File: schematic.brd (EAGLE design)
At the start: 100 x 70 mm, 44 parts, among them U1 ADP3338AKCZ-3.3RL7

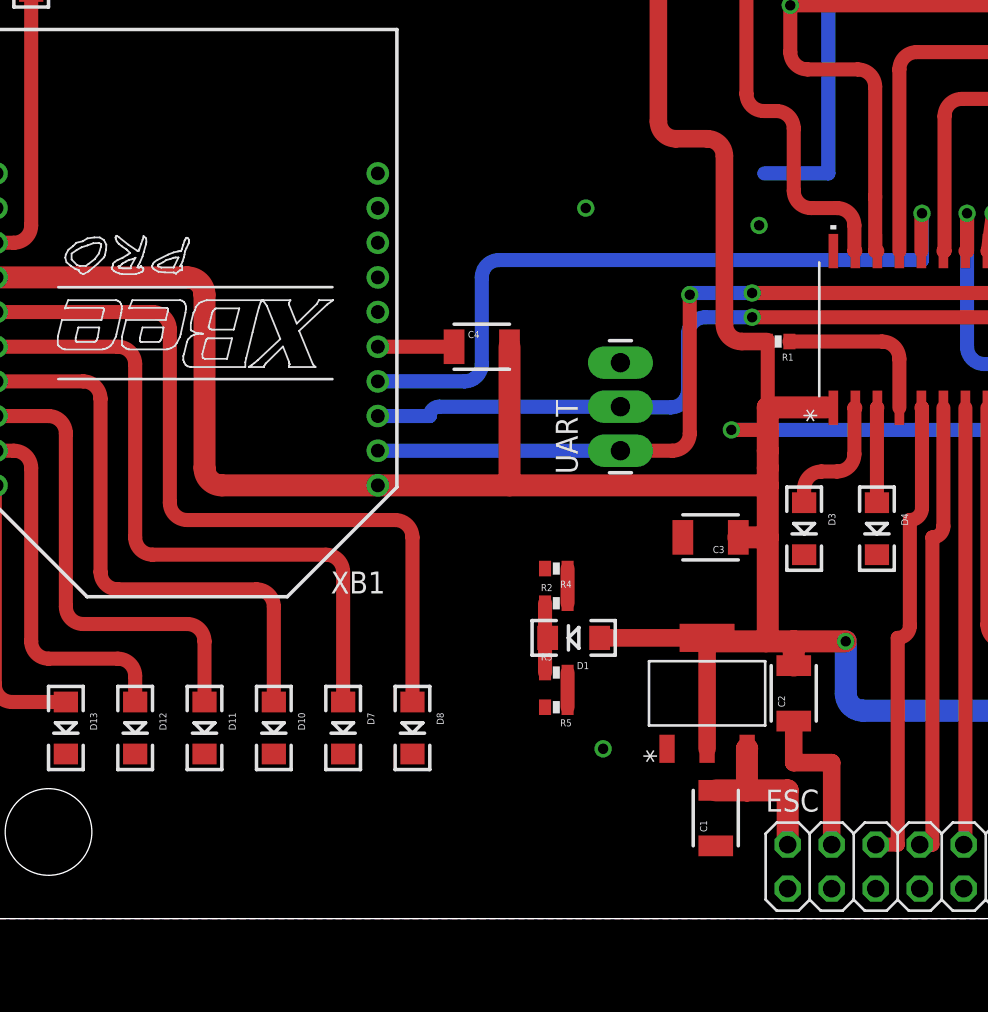
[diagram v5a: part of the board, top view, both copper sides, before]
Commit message: Added designer's name to pcb
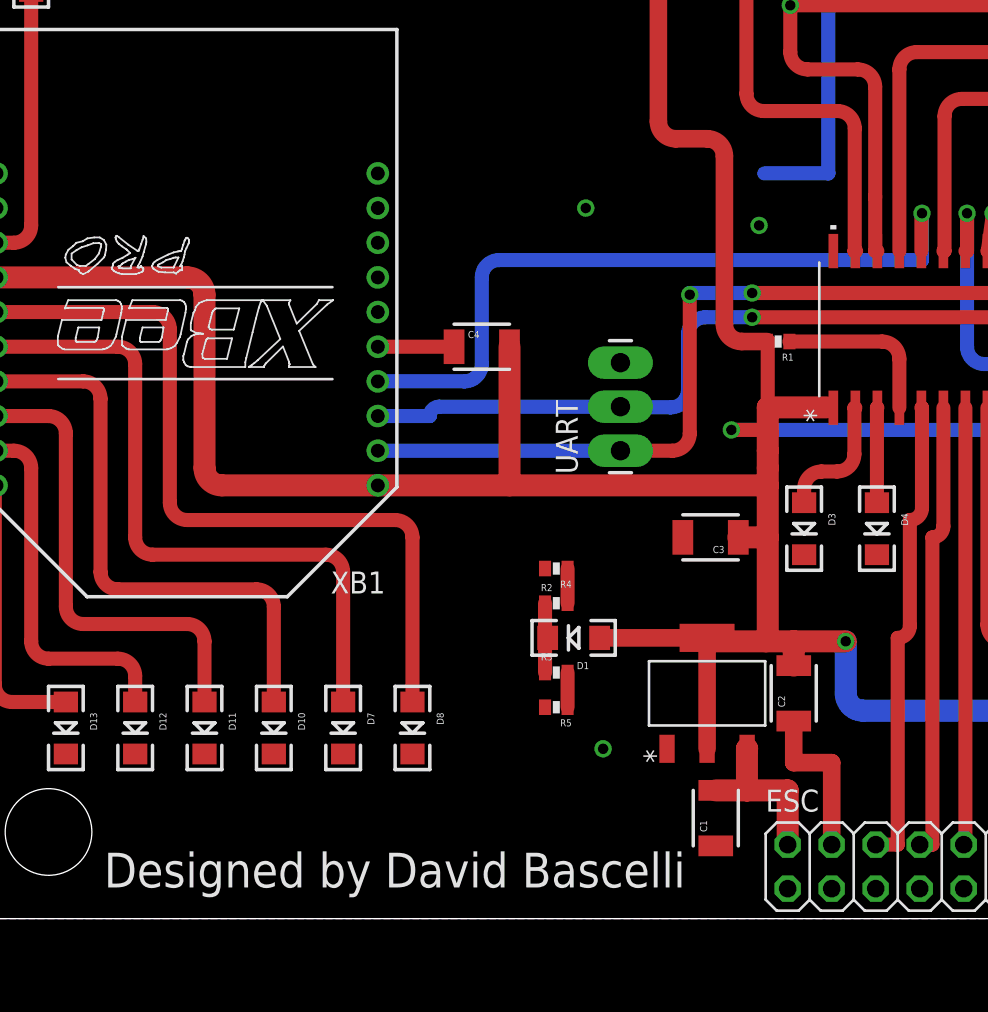
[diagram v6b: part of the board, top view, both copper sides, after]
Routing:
- net PGD/PITCH: track 57.0 -> 58.3 mm
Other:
- board text added: "Designed by David Bascelli"
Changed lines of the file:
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@@
 <rectangle x1="86.98" y1="19.7" x2="87.26" y2="19.74" layer="21" rot="R90"/>
 <rectangle x1="86.76" y1="42.76" x2="87.48" y2="42.8" layer="21" rot="R90"/>
+<text x="8.2" y="1.8" size="2" layer="21">Designed by David Bascelli</text>
 </plain>
 <attributes>
@@
 <contactref element="MAIN_CONTROLLER" pad="19"/>
 <wire x1="51.555" y1="38.5212" x2="51.5" y2="38.5212" width="0.8128" layer="1"/>
-<wire x1="47" y1="46.6" x2="46.27" y2="46.6" width="0.8128" layer="1"/>
 <wire x1="46.27" y1="46.6" x2="45.27" y2="47.6" width="0.8128" layer="1" curve="-90"/>
 <wire x1="45.27" y1="47.6" x2="45.27" y2="57.5" width="0.8128" layer="1"/>
 <wire x1="45.27" y1="57.5" x2="45.27" y2="68.19" width="0.8128" layer="1"/>
-<wire x1="48" y1="45.6" x2="48" y2="42" width="0.8128" layer="1"/>
-<wire x1="48" y1="42" x2="49" y2="41" width="0.8128" layer="1" curve="90"/>
-<wire x1="49" y1="41" x2="50.5" y2="41" width="0.8128" layer="1"/>
-<wire x1="50.5" y1="41" x2="51.5" y2="40" width="0.8128" layer="1" curve="-90"/>
-<wire x1="51.5" y1="40" x2="51.5" y2="38.5212" width="0.8128" layer="1"/>
-<wire x1="48" y1="45.6" x2="47" y2="46.6" width="0.8128" layer="1" curve="90"/>
 <wire x1="45.27" y1="57.5" x2="57.73" y2="57.5" width="0.8128" layer="1"/>
 <wire x1="57.73" y1="57.5" x2="58.73" y2="58.5" width="0.8128" layer="1" curve="90"/>
 <wire x1="58.73" y1="58.5" x2="58.73" y2="68" width="0.8128" layer="1"/>
+<wire x1="46.27" y1="46.6" x2="50.52" y2="46.6" width="0.8128" layer="1"/>
+<wire x1="50.52" y1="46.6" x2="51.52" y2="45.6" width="0.8128" layer="1" curve="-90"/>
+<wire x1="51.52" y1="45.6" x2="51.52" y2="38.52" width="0.8128" layer="1"/>
+<wire x1="51.52" y1="38.48" x2="51.52" y2="38.52" width="0.8128" layer="1"/>
+<wire x1="51.52" y1="38.52" x2="51.6" y2="38.52" width="0.8128" layer="1"/>
+<wire x1="51.52" y1="38.52" x2="51.5" y2="38.5212" width="0" layer="19" extent="1-1"/>
 </signal>
 <signal name="PGC/ROLL">

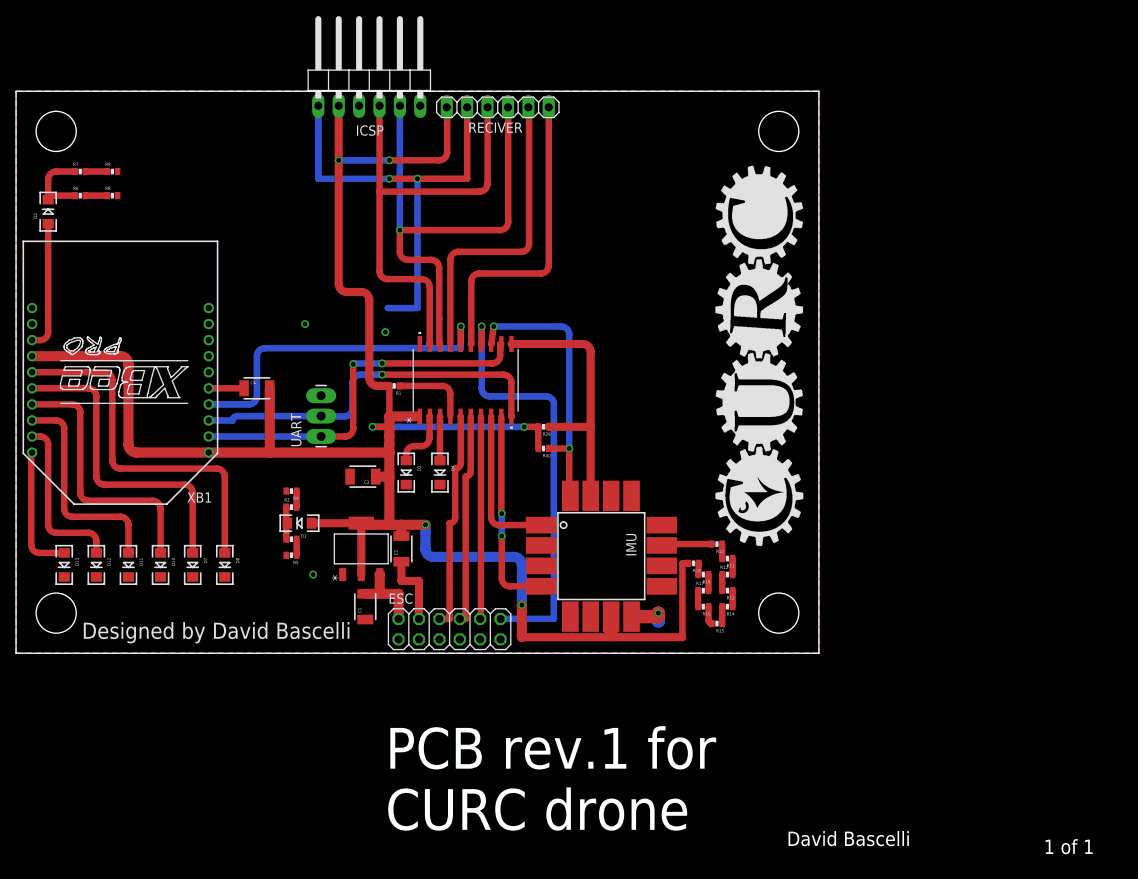
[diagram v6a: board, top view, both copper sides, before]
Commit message: Cleaned up the silkscreen and added more labels
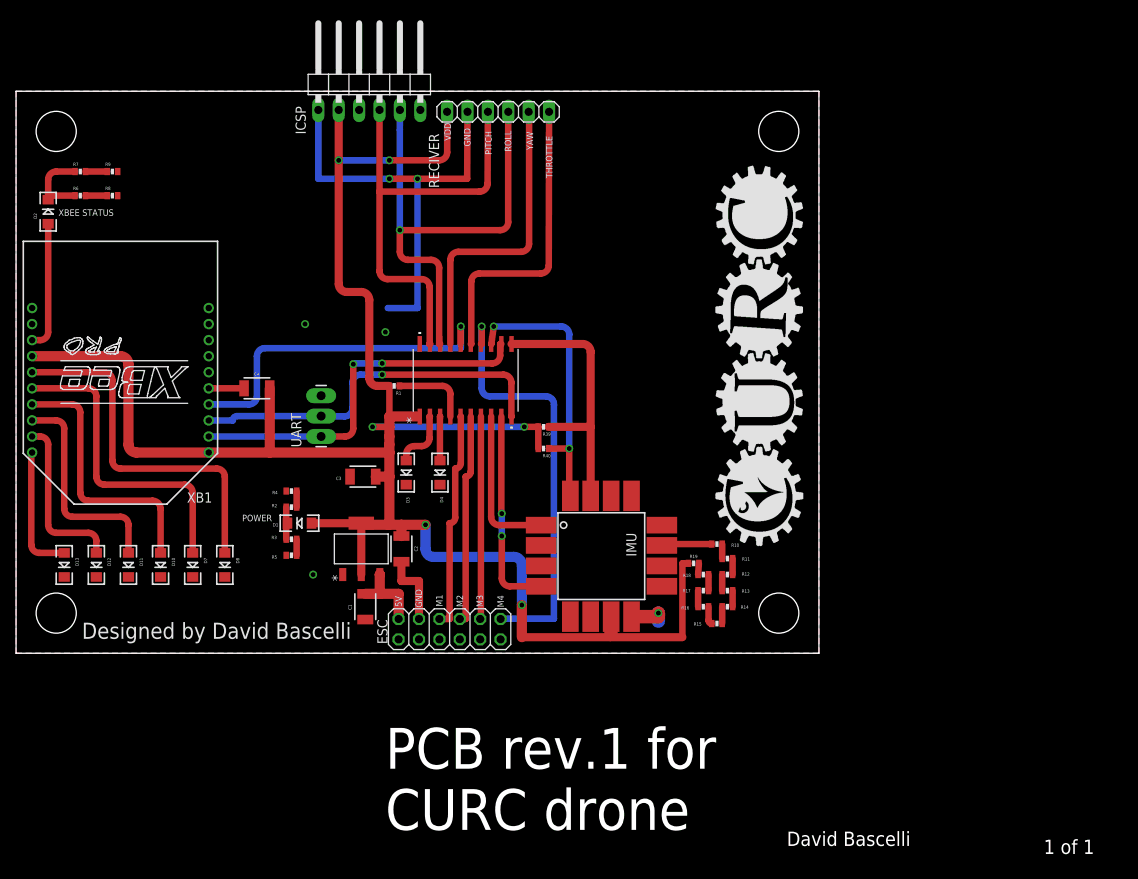
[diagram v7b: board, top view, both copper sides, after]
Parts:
- moved RECIVER 0.56 mm to (60.0, 67.4)
- moved ICSP 0.52 mm to (44.0, 71.5)
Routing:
- net PGD/PITCH: track 58.3 -> 57.2 mm
- net GND: track 70.4 -> 69.4 mm
- net THROTTLE: track 38.0 -> 37.5 mm
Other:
- board text added: "5V"
- board text added: "GND"
- board text added: "M1"
- board text added: "M2"
- board text added: "M3"
- board text added: "M4"
- board text added: "PITCH"
- board text added: "POWER"
- board text added: "ROLL"
- board text added: "THROTTLE"
- board text added: "VDD"
- board text added: "XBEE STATUS"
- board text added: "YAW"

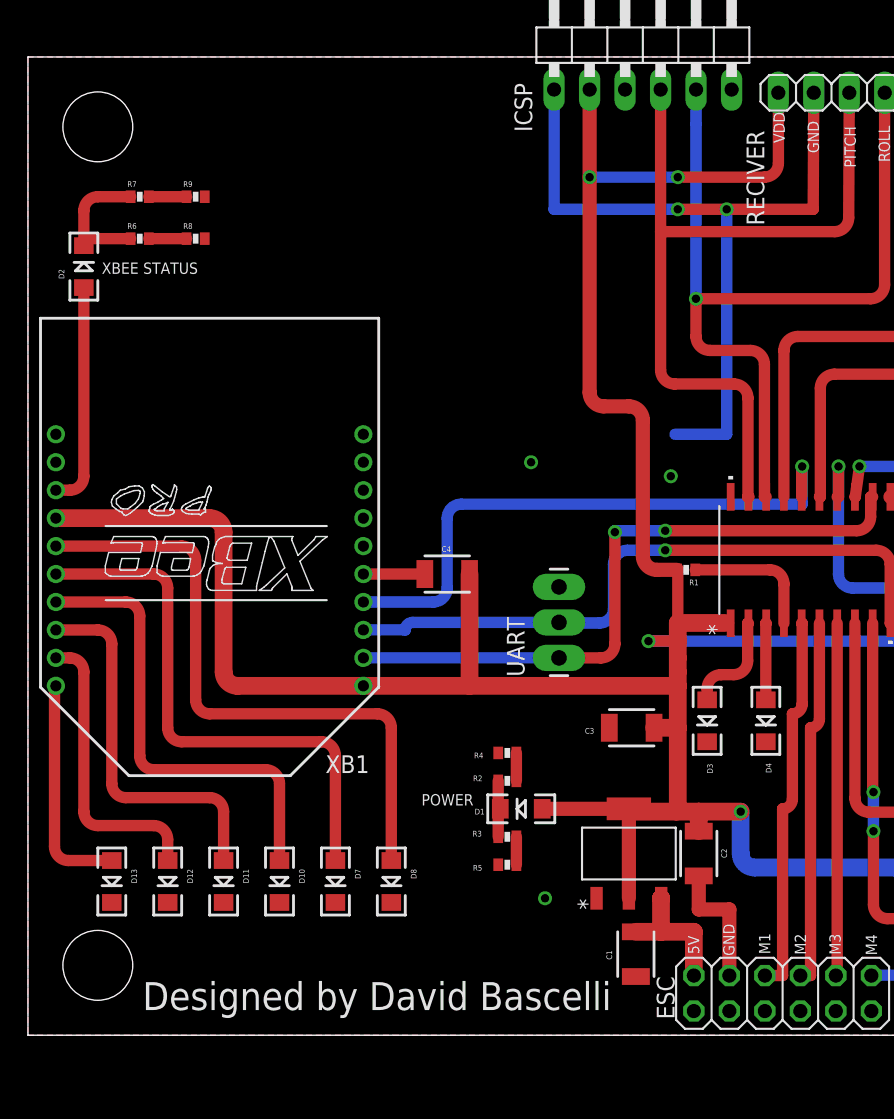
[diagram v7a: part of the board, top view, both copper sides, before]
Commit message: Fixed a mixup in the pinout for the ICSP
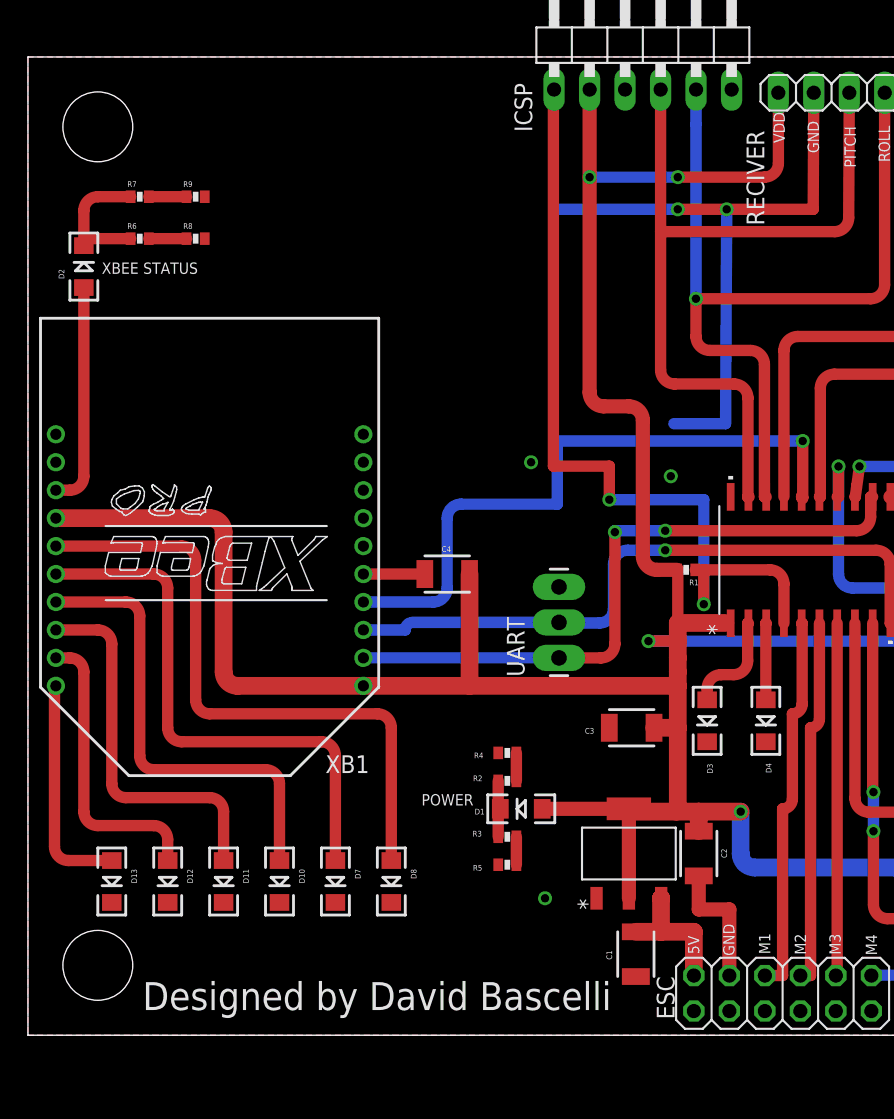
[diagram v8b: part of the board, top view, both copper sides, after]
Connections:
- removed net VSS: ICSP.3
- net GND: now also ICSP.3; no longer ICSP.1
- net VPP: now also ICSP.1
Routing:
- net VPP: track 9.58 -> 59.7 mm, vias 0 -> 2
- net GND: track 69.4 -> 60.0 mm
- net XBEE_INT: track 42.1 -> 46.1 mm
